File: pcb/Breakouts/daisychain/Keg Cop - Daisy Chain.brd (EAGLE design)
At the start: 33.2 x 43.2 mm, 3 parts

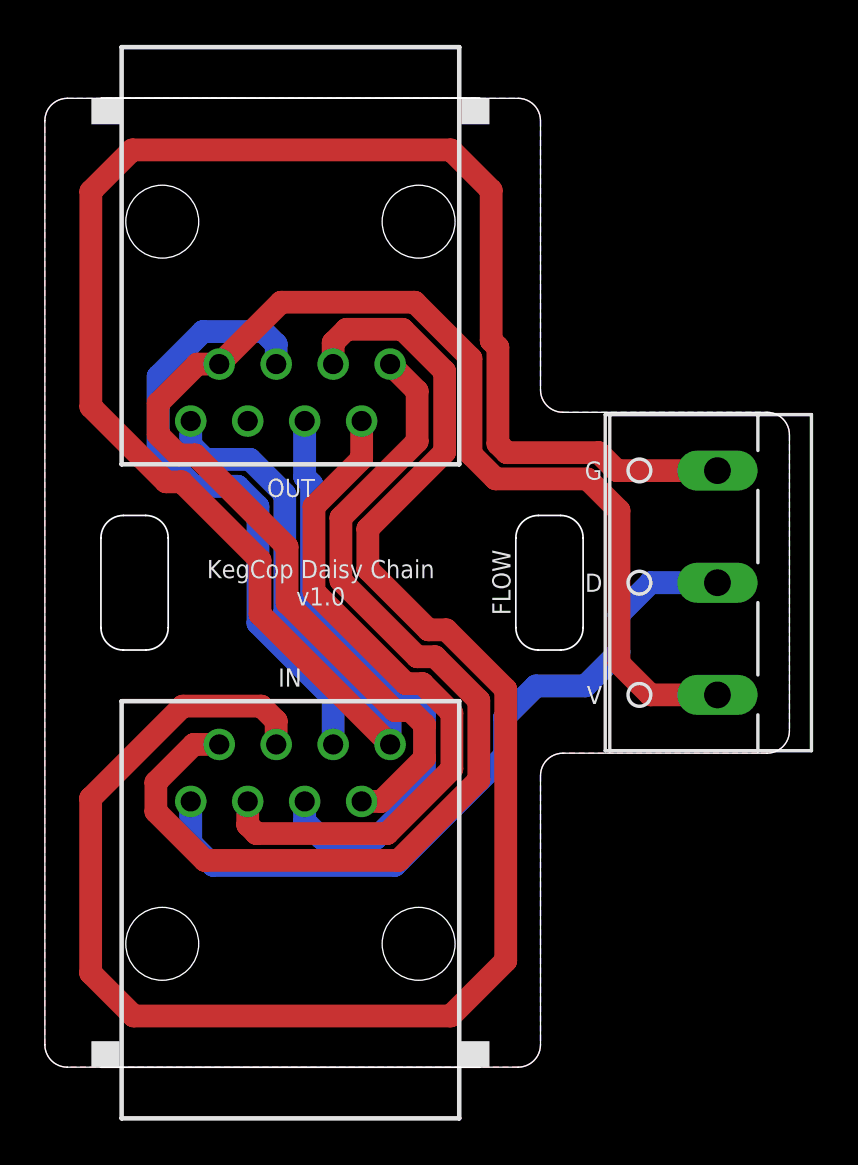
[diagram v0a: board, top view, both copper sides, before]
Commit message: Rewire, move to 9 meters
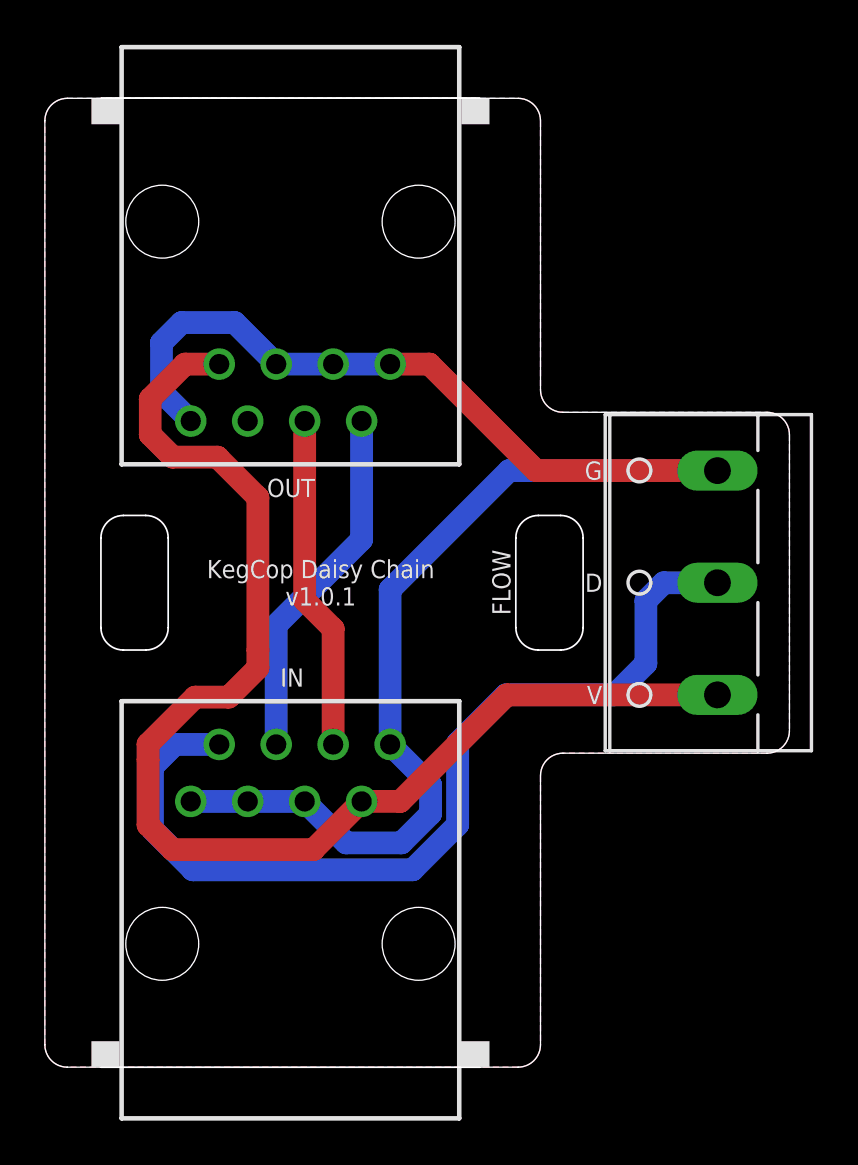
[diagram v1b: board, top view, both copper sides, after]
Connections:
- net 5V renamed 5VD
- removed net DATA: FLOW.2, IN.1
- removed net N$1: IN.2, OUT.1
- removed net N$2: IN.3, OUT.2
- removed net N$3: IN.4, OUT.3
- removed net N$5: IN.5, OUT.4
- removed net N$7: IN.6, OUT.5
- new net DATA0: FLOW.2, IN.2
- new net DATA1: IN.4, OUT.2
- new net DATA2: IN.6, OUT.4
- net GND: now also IN.1, IN.3, IN.5, OUT.1, OUT.3, OUT.5
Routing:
- net N$3: track 77.1 -> 0.00 mm
- net N$1: track 45.1 -> 0.00 mm
- net DATA0: track 0.00 -> 41.2 mm
- net DATA: track 33.0 -> 0.00 mm
- net N$2: track 30.9 -> 0.00 mm
- net N$7: track 28.0 -> 0.00 mm
- net N$5: track 26.1 -> 0.00 mm
- net GND: track 90.9 -> 71.5 mm
- net DATA1: track 0.00 -> 16.0 mm
- net DATA2: track 0.00 -> 14.9 mm
- net 5VD: track 65.7 -> 57.5 mm
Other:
- board text added: "KegCop Daisy Chain v1.0.1"
- board text removed: "KegCop Daisy Chain v1.0"
